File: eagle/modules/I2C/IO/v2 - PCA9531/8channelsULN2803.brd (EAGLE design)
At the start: 113 x 82.5 mm, 57 parts, among them IC1 PCA9531

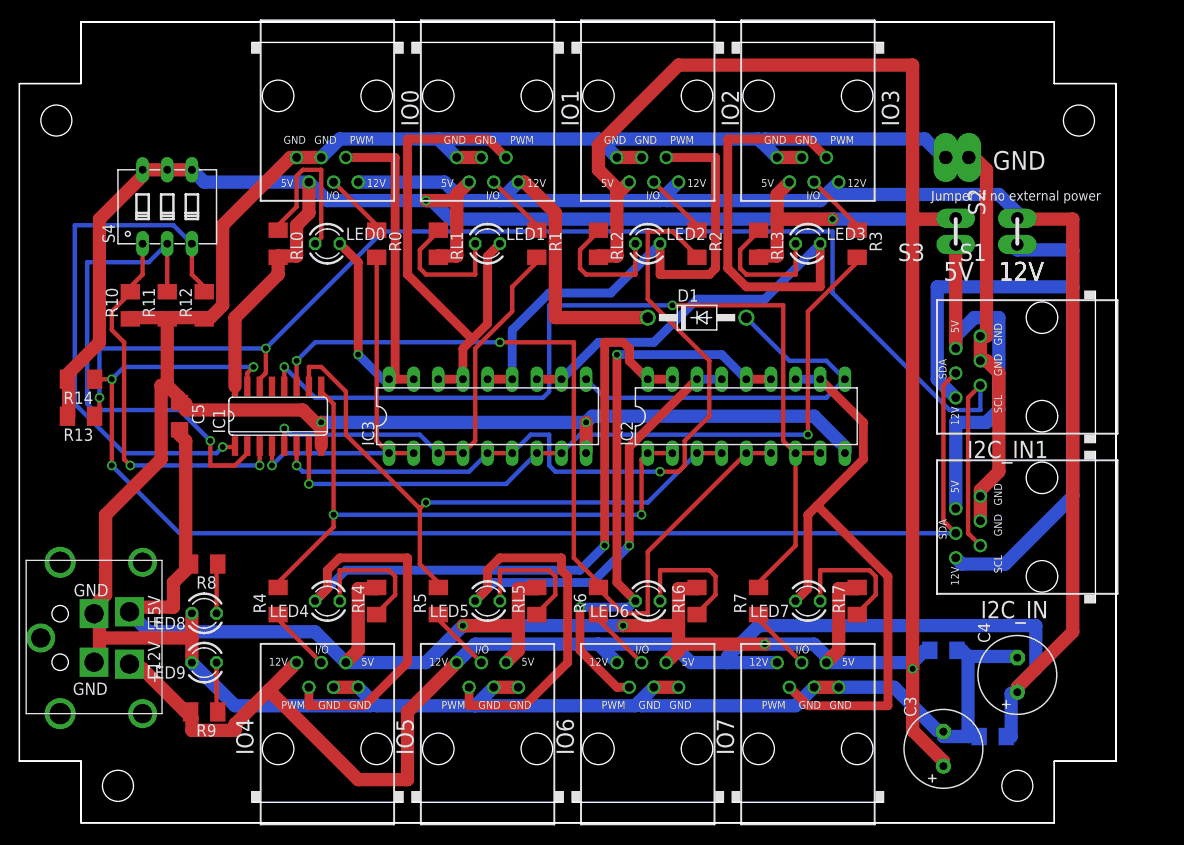
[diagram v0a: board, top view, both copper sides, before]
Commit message: correction of RESET to I2C component
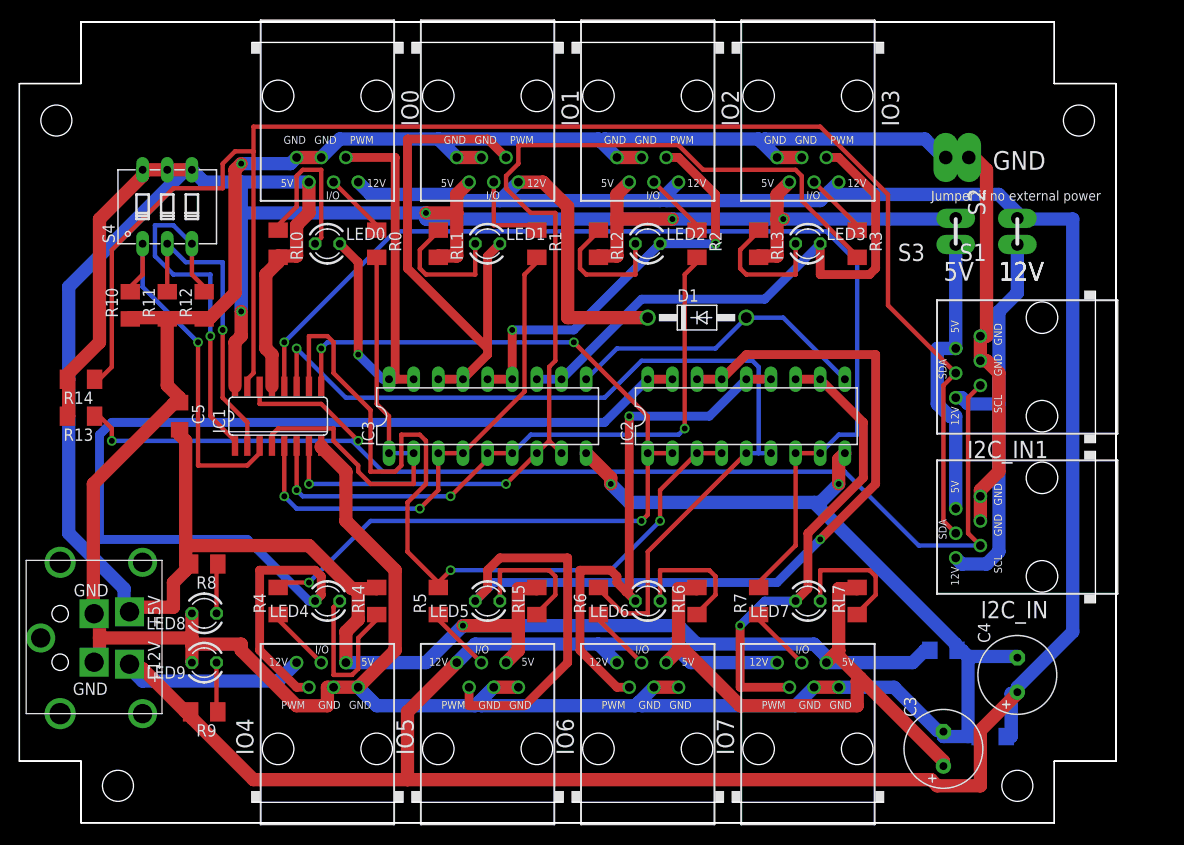
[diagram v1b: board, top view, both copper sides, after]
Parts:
- R13, R14: value reserve -> 10k
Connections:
- net +5V: now also IC1.13
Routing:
- net +12V: track 300.7 -> 340.5 mm
- net N$42: track 77.6 -> 116.3 mm
- net SDA: track 135.5 -> 168.9 mm, vias 3 -> 0
- net N$5: track 73.1 -> 42.4 mm
- net P4: track 64.5 -> 95.2 mm, vias 2 -> 4
- net P3: track 77.8 -> 108.5 mm
- net N$8: track 99.7 -> 121.4 mm, vias 1 -> 0
- net P5: track 64.5 -> 86.1 mm, vias 1 -> 2
- net N$17: track 50.5 -> 31.5 mm
- net N$16: track 55.7 -> 38.5 mm
- net N$44: track 64.7 -> 48.3 mm, vias 0 -> 1
- net N$9: track 74.0 -> 58.4 mm
- net P2: track 81.6 -> 66.3 mm, vias 2 -> 3
- net P7: track 97.6 -> 110.0 mm, vias 2 -> 1
- net N$7: track 40.6 -> 30.3 mm
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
